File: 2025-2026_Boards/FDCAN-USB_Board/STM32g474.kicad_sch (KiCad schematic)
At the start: 14 parts, among them J4 Conn_01x02_Pin, J5 Conn_01x02_Pin, J6 Conn_ARM_JTAG_SWD_10, U3 STM32G474CETx

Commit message: microcontroller pin update
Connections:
- net LED_Debug1: now also U3.2 (PC13); no longer U3.9 (PA1)
- net LED_Debug2: now also U3.4 (PC15); no longer U3.10 (PA2)
- net LED_RX_1: now also U3.10 (PA2); no longer U3.13 (PA5)
- net LED_RX_2: now also U3.14 (PA6); no longer U3.17 (PB1)
- net LED_TX_1: now also U3.12 (PA4); no longer U3.14 (PA6)
- net USB_N renamed USB_DM
- net USB_P renamed USB_DP

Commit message: grouped components
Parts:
- R13: footprint Resistor_SMD:R_0402_1005Metric -> Resistor_SMD:R_0603_1608Metric
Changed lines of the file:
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@@
 			)
 		)
-		(property "Footprint" "Resistor_SMD:R_0402_1005Metric"
+		(property "Footprint" "Resistor_SMD:R_0603_1608Metric"
 			(at 170.942 101.6 90)
 			(effects

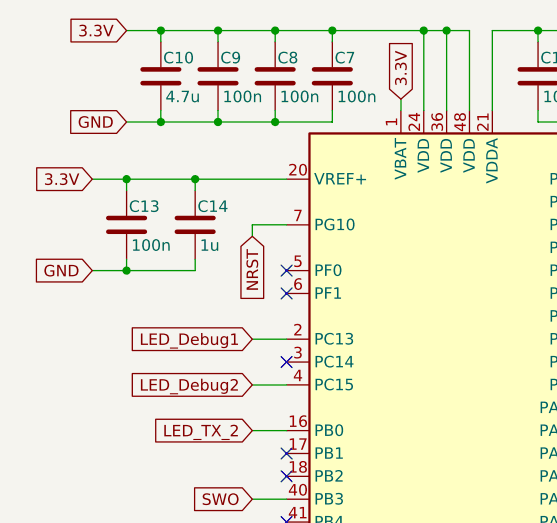
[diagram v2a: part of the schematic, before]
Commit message: Finished arranging components
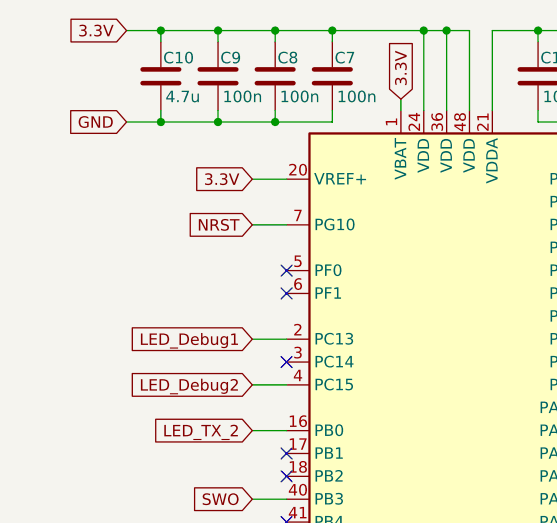
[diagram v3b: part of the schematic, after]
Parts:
- removed C13: 100n, Capacitor_SMD:C_0402_1005Metric, symbol Device:C
- removed C14: 1u, Capacitor_SMD:C_0402_1005Metric, symbol Device:C

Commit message: Layout finished
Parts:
- removed J4: Conn_01x02_Pin, Connector_PinHeader_2.54mm:PinHeader_1x02_P2.54mm_Vertical, symbol Connector:Conn_01x02_Pin
- removed R13: 10k, Resistor_SMD:R_0603_1608Metric, symbol Device:R
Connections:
- net BOOT0 is gone; now on net CAN_RX1: U3.45 (PB8)
- net CAN_RX1: no longer U3.26 (PB12)
- net CAN_RX2: now also U3.42 (PB5); no longer U3.30 (PA8)
- net CAN_TX1: now also U3.46 (PB9); no longer U3.27 (PB13)
- net CAN_TX2: now also U3.43 (PB6); no longer U3.39 (PA15)
- net LED_Debug1: now also U3.26 (PB12); no longer U3.2 (PC13)
- net LED_Debug2: now also U3.25 (PB11); no longer U3.4 (PC15)
- net LED_RX_1: now also U3.9 (PA1); no longer U3.10 (PA2)
- net LED_RX_2: now also U3.12 (PA4); no longer U3.14 (PA6)
- net LED_TX_1: now also U3.10 (PA2); no longer U3.12 (PA4)
- net LED_TX_2: now also U3.13 (PA5); no longer U3.16 (PB0)
- net LED_TX_3: now reaches U3.17 (PB1)
- net USB_DM renamed USB_N
- net USB_DP renamed USB_P
- new net CAN_RX3: U3.30 (PA8)
- new net CAN_TX3: U3.39 (PA15)
- new net LED_RX_3: U3.16 (PB0)
- no-connect marks 22 -> 19
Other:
- moved on the sheet: C15, J5, J6

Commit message: Gerber files, BOM, layout fix
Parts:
- C11: value 10n -> 100n
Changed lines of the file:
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@@
 			)
 		)
-		(property "Value" "10n"
+		(property "Value" "100n"
 			(at 114.808 49.276 0)
 			(effects
